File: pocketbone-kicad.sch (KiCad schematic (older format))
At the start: 62 parts, among them P1 USB_OTG, P2 USB_OTG, P3 CONN_01X10, P4 CONN_02X02, SW1 SW_PUSH_SMALL_H, SW2 SW_PUSH_SMALL_H, U1 SN74LVC1G07, U2 OSD3358, U3 24LC32AT-I/OT, U4 TPS2051C, Y2 24MHz

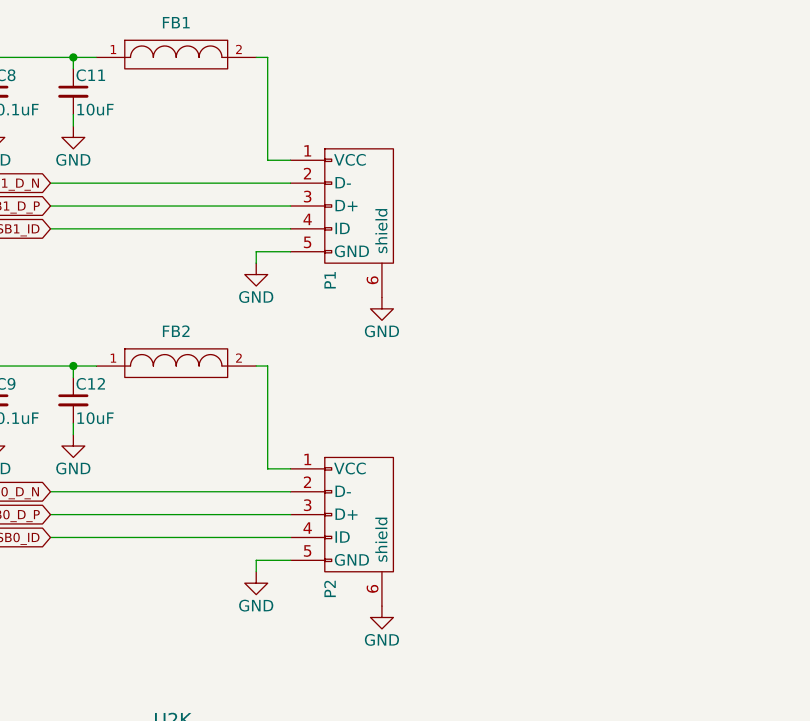
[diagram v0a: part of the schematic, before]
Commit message: Updated Footprint and Schematic Librarys
The Paths of the USB and SOT Footprints pointed to local Directorys on
your HDD instead of the Project Folder
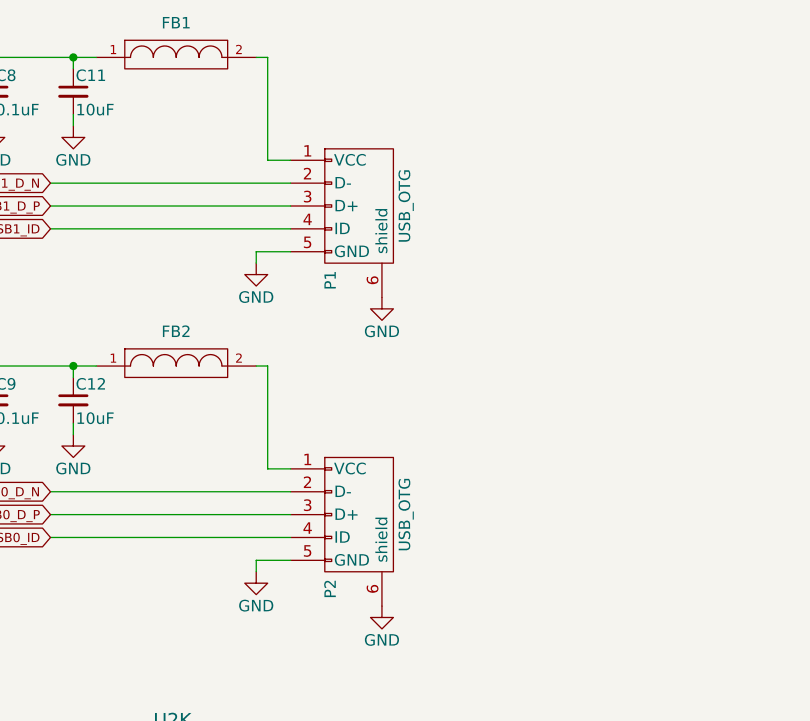
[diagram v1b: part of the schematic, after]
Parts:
- P1, P2: footprint Sensors:USB_MICRO_B_ST-USB-001E -> pocketbone-kicad:USB_MICRO_B_ST-USB-001E
- U1, U3, U4: footprint Housings_SOT-23_SOT-143_TSOT-6:SOT-23-5 -> pocketbone-kicad:SOT-23-5
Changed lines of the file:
@@
 EESchema Schematic File Version 2
-LIBS:pocketbone-kicad-rescue
 LIBS:power
 LIBS:device
@@
 LIBS:contrib
 LIBS:valves
-LIBS:pocketbone-kicad
 LIBS:pocketbone-kicad-cache
 EELAYER 25 0
@@
 	12   12025 12300
 	1    0    0    -1
-$EndComp
-$Comp
-L USB_OTG-RESCUE-pocketbone-kicad P1
-U 1 1 58337CB9
-P 9700 9500
-F 0 "P1" H 10025 9375 50  0000 C CNN
-F 1 "USB_OTG" H 9700 9700 50  0001 C CNN
-F 2 "Sensors:USB_MICRO_B_ST-USB-001E" V 9650 9400 50  0001 C CNN
-F 3 "" V 9650 9400 50  0000 C CNN
-	1    9700 9500
-	0    1    1    0
-$EndComp
-$Comp
-L USB_OTG-RESCUE-pocketbone-kicad P2
-U 1 1 58338BA7
-P 9700 10850
-F 0 "P2" H 10025 10725 50  0000 C CNN
-F 1 "USB_OTG" H 9700 11050 50  0001 C CNN
-F 2 "Sensors:USB_MICRO_B_ST-USB-001E" V 9650 10750 50  0001 C CNN
-F 3 "" V 9650 10750 50  0000 C CNN
-	1    9700 10850
-	0    1    1    0
 $EndComp
 Text GLabel 4500 8900 2    40   BiDi ~ 0
@@
 F 0 "U1" H 1700 4800 60  0000 C CNN
 F 1 "SN74LVC1G07" H 1950 4400 60  0000 C CNN
-F 2 "Housings_SOT-23_SOT-143_TSOT-6:SOT-23-5" H 1980 4600 60  0001 C CNN
+F 2 "pocketbone-kicad:SOT-23-5" H 1980 4600 60  0001 C CNN
 F 3 "" H 1980 4600 60  0000 C CNN
 	1    1950 4600
@@
 F 0 "U3" H 3250 12500 50  0000 C CNN
 F 1 "24LC32AT-I/OT" H 3450 12100 50  0000 C CNN
-F 2 "Housings_SOT-23_SOT-143_TSOT-6:SOT-23-5" H 3450 12100 50  0001 C CIN
+F 2 "pocketbone-kicad:SOT-23-5" H 3450 12100 50  0001 C CIN
 F 3 "" H 3450 12250 50  0000 C CNN
 	1    3450 12250
@@
 F 0 "U4" H 6450 9150 60  0000 C CNN
 F 1 "TPS2051C" H 6650 8750 60  0000 C CNN
-F 2 "Housings_SOT-23_SOT-143_TSOT-6:SOT-23-5" H 6650 8950 60  0001 C CNN
+F 2 "pocketbone-kicad:SOT-23-5" H 6650 8950 60  0001 C CNN
 F 3 "" H 6650 8950 60  0000 C CNN
 	1    6650 8950
@@
 	2250 2150 2400 2150
 $Comp
-L GND #PWR?
+L GND #PWR042
 U 1 1 589C02FE
 P 2400 2350
-F 0 "#PWR?" H 2400 2100 50  0001 C CNN
+F 0 "#PWR042" H 2400 2100 50  0001 C CNN
 F 1 "GND" H 2400 2200 50  0000 C CNN
 F 2 "" H 2400 2350 50  0000 C CNN
@@
 	2400 2250 2400 2350
 $Comp
-L GND #PWR?
+L GND #PWR043
 U 1 1 589CA027
 P 9800 11250
-F 0 "#PWR?" H 9800 11000 50  0001 C CNN
+F 0 "#PWR043" H 9800 11000 50  0001 C CNN
 F 1 "GND" H 9800 11100 50  0000 C CNN
 F 2 "" H 9800 11250 50  0000 C CNN
@@
 $EndComp
 $Comp
-L GND #PWR?
+L GND #PWR044
 U 1 1 589CA10D
 P 9800 9900
-F 0 "#PWR?" H 9800 9650 50  0001 C CNN
+F 0 "#PWR044" H 9800 9650 50  0001 C CNN
 F 1 "GND" H 9800 9750 50  0000 C CNN
 F 2 "" H 9800 9900 50  0000 C CNN
@@
 	1    0    0    -1
 $EndComp
+$Comp
+L USB_OTG-RESCUE-pocketbone-kicad P1
+U 1 1 58A2CCA0
+P 9700 9500
+F 0 "P1" H 10025 9375 50  0000 C CNN
+F 1 "USB_OTG" H 9700 9700 50  0000 C CNN
+F 2 "pocketbone-kicad:USB_MICRO_B_ST-USB-001E" V 9650 9400 50  0001 C CNN
+F 3 "" V 9650 9400 50  0000 C CNN
+	1    9700 9500
+	0    1    1    0
+$EndComp
+$Comp
+L USB_OTG-RESCUE-pocketbone-kicad P2
+U 1 1 58A2DE0A
+P 9700 10850
+F 0 "P2" H 10025 10725 50  0000 C CNN
+F 1 "USB_OTG" H 9700 11050 50  0000 C CNN
+F 2 "pocketbone-kicad:USB_MICRO_B_ST-USB-001E" V 9650 10750 50  0001 C CNN
+F 3 "" V 9650 10750 50  0000 C CNN
+	1    9700 10850
+	0    1    1    0
+$EndComp
 $EndSCHEMATC
